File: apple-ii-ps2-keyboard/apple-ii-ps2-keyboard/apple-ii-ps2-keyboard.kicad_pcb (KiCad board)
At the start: 2 copper layers, 59.2 x 51.3 mm, 23 parts, among them J1 PS/2, J2 apple-ii

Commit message: * add shift button IO control for later * add the A0-A7 and power pins as expansion headers if I want to do   anything else
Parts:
- added J3: SHIFT_KEY, Connector_PinHeader_2.54mm:PinHeader_1x01_P2.54mm_Vertical, F.Cu at (15.7, 17.5)
- added J4: EXP, Connector_PinHeader_2.54mm:PinHeader_1x08_P2.54mm_Vertical, F.Cu at (15.5, 30.0)
- added J5: EXP_PWR, Connector_PinHeader_2.54mm:PinHeader_1x02_P2.54mm_Vertical, F.Cu at (15.5, 56.4)
- moved R13 3.82 mm to (66.0, 49.3)
- moved C2 3.82 mm to (71.4, 28.4)
- moved D1 3.82 mm to (71.4, 22.6)
- moved D3 3.82 mm to (70.4, 16.0)
- moved R10 3.82 mm to (47.8, 44.5)
- moved R11 3.82 mm to (45.2, 44.5)
- moved R2 3.82 mm to (57.9, 22.4)
- moved R3 3.82 mm to (55.4, 22.4)
- moved R4 3.82 mm to (50.3, 22.4)
- moved R5 3.82 mm to (47.8, 22.4)
- moved R6 3.82 mm to (45.2, 22.4)
- moved R8 3.82 mm to (52.8, 44.5)
- moved R9 3.82 mm to (50.3, 44.5)
- moved A1 3.82 mm to (35.8, 57.9)
- moved C1 3.82 mm to (65.0, 44.2)
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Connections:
- A1 pad 15: Net-(A1-Pad15) -> SHIFT_KEY
- A1 pad 19: Net-(A1-Pad19) -> A0
- A1 pad 20: Net-(A1-Pad20) -> A1
- A1 pad 21: Net-(A1-Pad21) -> A2
- A1 pad 22: Net-(A1-Pad22) -> A3
- A1 pad 23: Net-(A1-Pad23) -> A4
- A1 pad 24: Net-(A1-Pad24) -> A5
- A1 pad 25: Net-(A1-Pad25) -> A6
- A1 pad 26: Net-(A1-Pad26) -> A7
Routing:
- net SHIFT_KEY: track 0.00 -> 24.0 mm, vias 0 -> 1
- net KBD_VCC: track 111.4 -> 122.0 mm
- net DATA_6: track 21.5 -> 16.1 mm
- net A7: track 0.00 -> 5.08 mm
- net A6: track 0.00 -> 5.08 mm
- net A5: track 0.00 -> 5.08 mm
- net A4: track 0.00 -> 5.08 mm
- net A3: track 0.00 -> 5.08 mm
- net A2: track 0.00 -> 5.08 mm
- net A1: track 0.00 -> 5.08 mm
- net A0: track 0.00 -> 5.08 mm
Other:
- board size 59.2 x 51.3 mm -> 63.2 x 51.3 mm
- board text added: "+"
- board text added: "Shift"
- board text removed: "V"

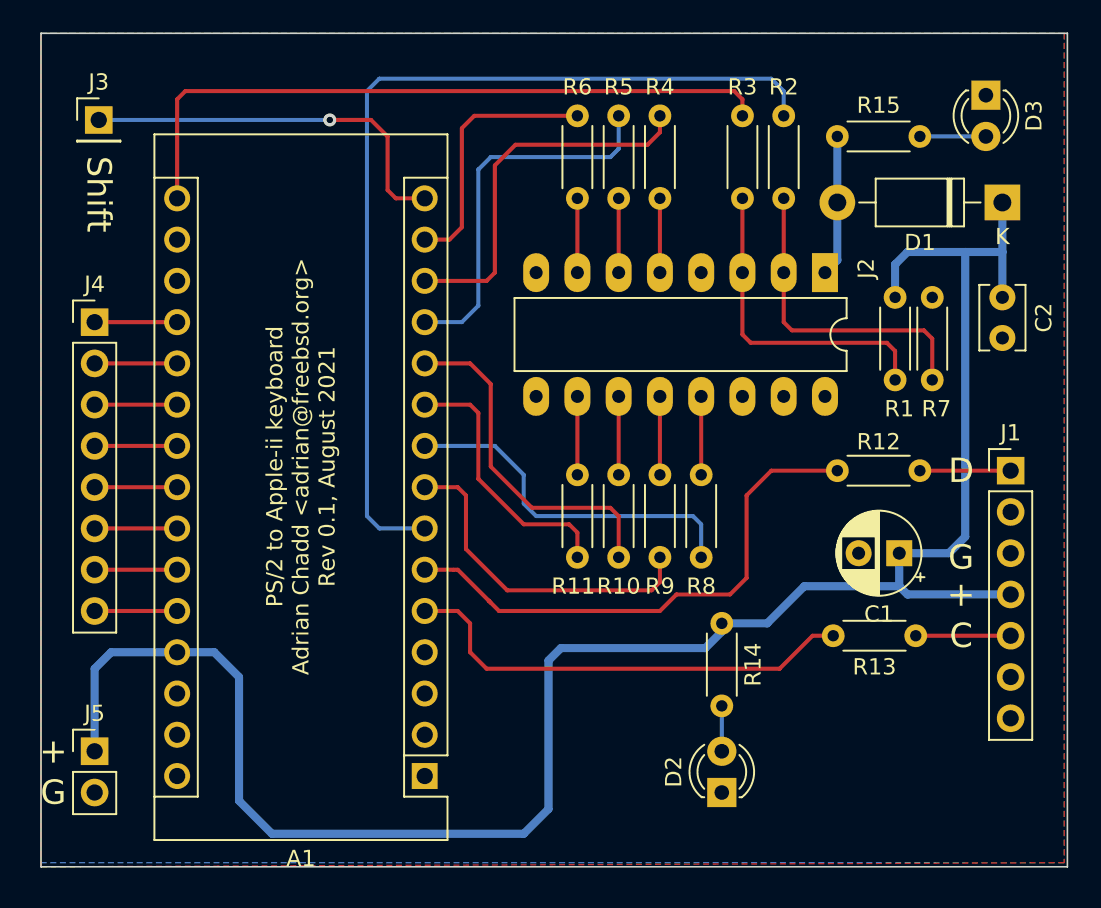
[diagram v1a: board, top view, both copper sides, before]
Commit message: * add uart connector * add pin 7 on the ps/2 connector as a ground, for shield
ok, this may be the thing I ship!
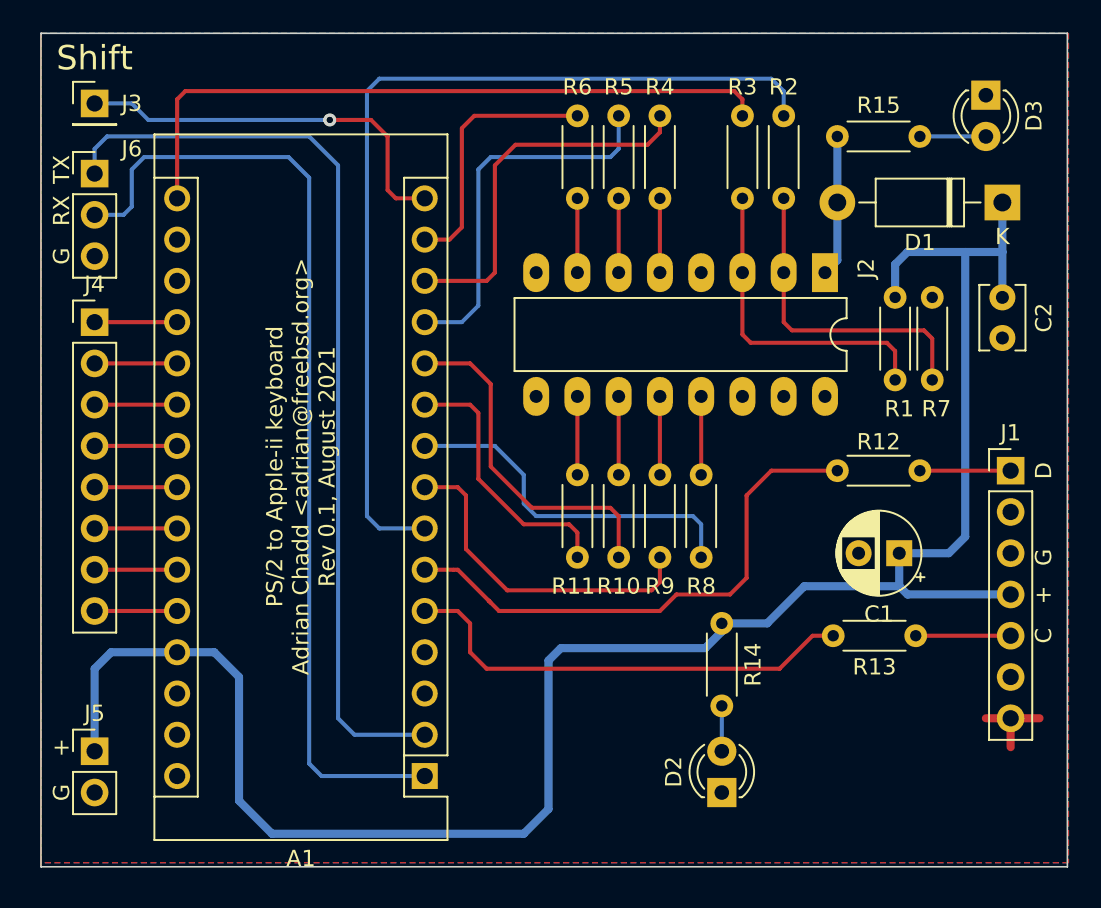
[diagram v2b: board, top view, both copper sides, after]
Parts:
- added J6: UART, Connector_PinHeader_2.54mm:PinHeader_1x03_P2.54mm_Vertical, F.Cu at (15.5, 20.8)
- moved J3 1.05 mm to (15.5, 16.5)
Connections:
- A1 pad 1: Net-(A1-Pad1) -> UART_TX
- A1 pad 2: Net-(A1-Pad2) -> UART_RX
- J1 pad 7: Net-(J1-Pad7) -> GND
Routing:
- net UART_TX: track 0.00 -> 60.0 mm
- net UART_RX: track 0.00 -> 57.4 mm
- net GND: track 0.00 -> 5.08 mm
- net SHIFT_KEY: track 24.0 -> 24.7 mm
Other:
- board text added: "RX"
- board text added: "TX"
